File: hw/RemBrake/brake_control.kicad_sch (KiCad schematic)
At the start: 33 parts, among them J7 Conn_01x07, J8 Conn_01x07, J9 Conn_01x03, Q6 BC337, Q7 BC847, U5 LM555xN

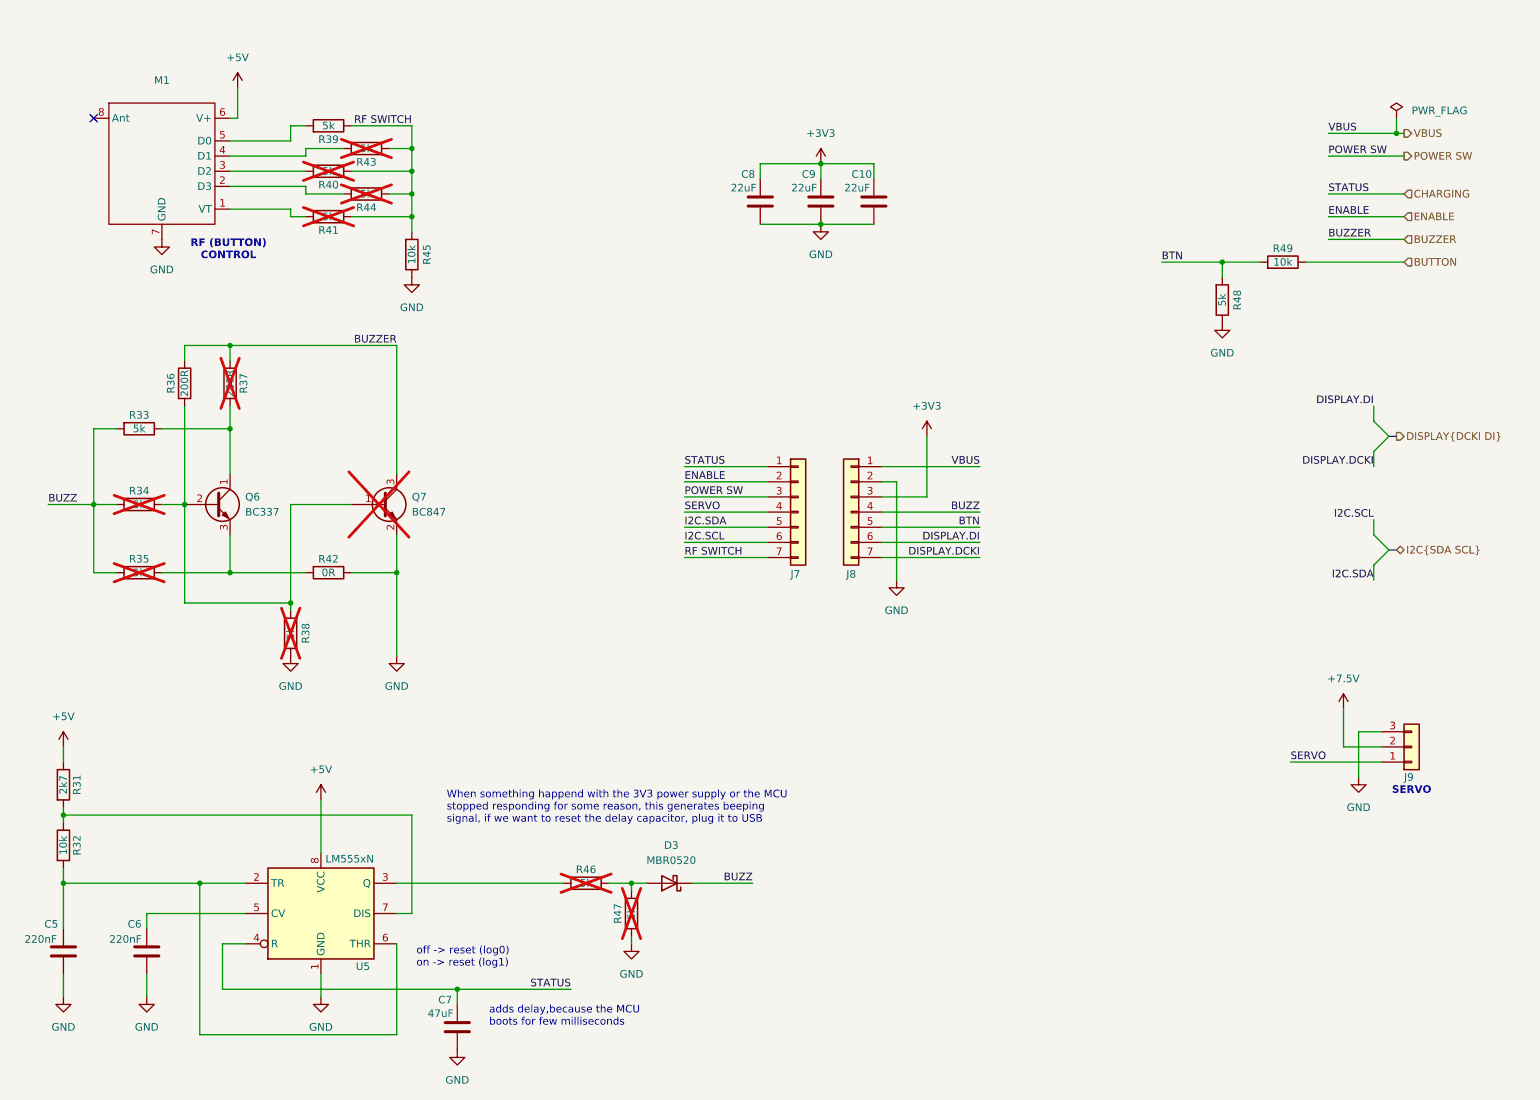
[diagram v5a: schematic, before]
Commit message: fixed bugs with LED reverse current leakage and beeper deterministic startup delay
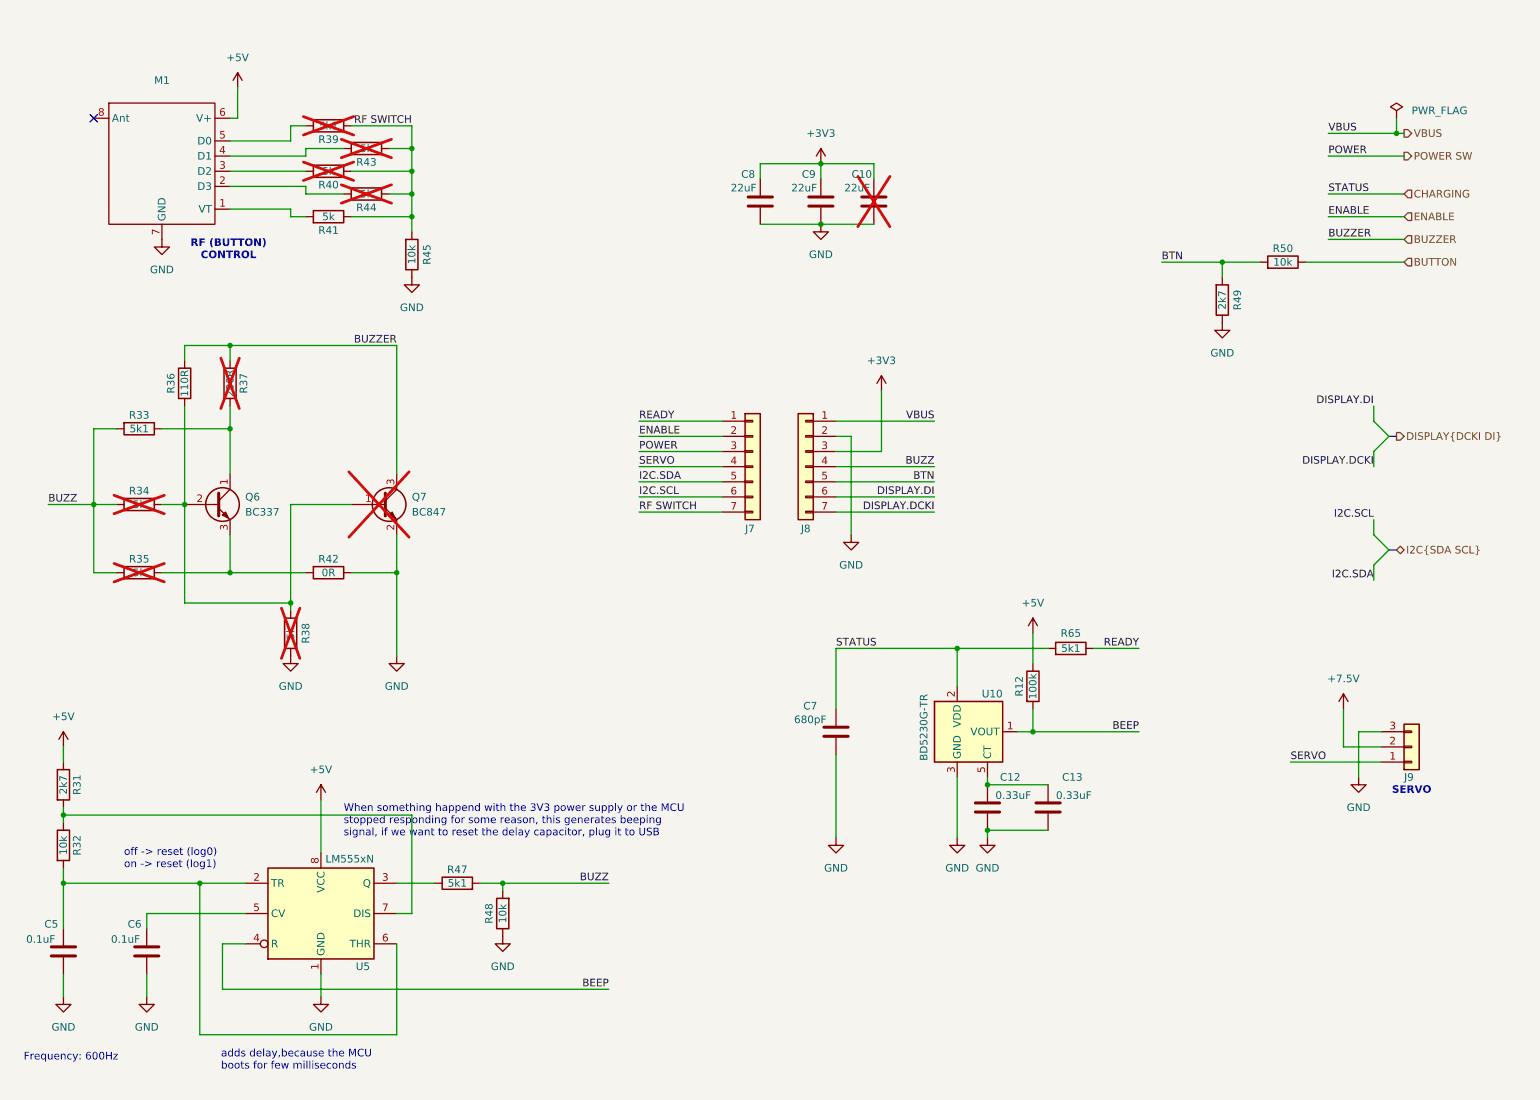
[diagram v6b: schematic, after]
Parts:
- removed D3: MBR0520, Diode_SMD:D_SOD-123, symbol Diode:MBR0520
- added C12, C13: 0.33uF, Capacitor_SMD:C_0805_2012Metric_Pad1.18x1.45mm_HandSolder, symbol Device:C
- added R12: 100k, Resistor_SMD:R_0805_2012Metric_Pad1.20x1.40mm_HandSolder, symbol Device:R
- added R65: 5k1, Resistor_SMD:R_0805_2012Metric_Pad1.20x1.40mm_HandSolder, symbol Device:R
- added U10: BD5230G-TR, Package_TO_SOT_SMD:SOT-23-6_Handsoldering, symbol dodo-power:BD5230G-TR
- C10: now not fitted
- C5, C6: value 220nF -> 0.1uF
- C7: value 47uF -> 680pF
- R33: value 5k -> 5k1
- R36: value 200R -> 110R
- R39: value 5k -> 5k1; now not fitted
- R41: now fitted
- R47: renamed from R46; value 5k -> 5k1; now fitted
- R48: renamed from R47; value 5k -> 10k; now fitted
- R49: renamed from R48; value 5k -> 2k7
- renumbered R49 to R50
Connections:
- net +5V: now also R12.1
- net BUZZ: now also R47.2, R48.2
- net CHARGING: now also R65.2, U10.2 (VDD); no longer J7.1 (Pin_1), U5.4 (R)
- net GND: now also C12.2, C13.2, U10.3 (GND)
- new net: C12.1, C13.1, U10.5 (CT)
- new net BEEP: R12.2, U10.1 (VOUT), U5.4 (R)
- new net READY: J7.1 (Pin_1), R65.1
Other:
- note added: "Frequency: 600Hz"
- moved on the sheet: J7, J8

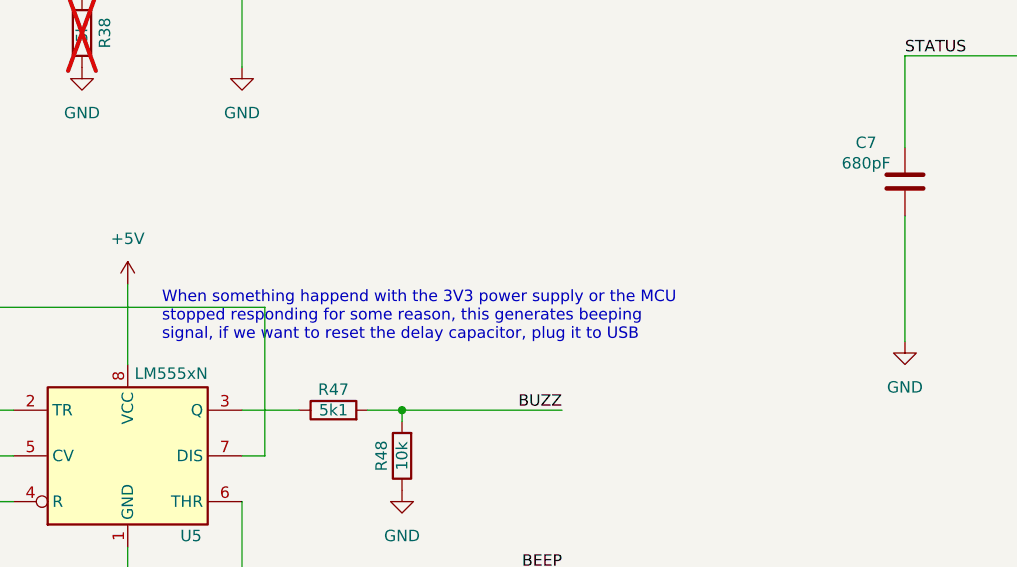
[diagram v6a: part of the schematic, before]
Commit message: updated pcb and added todo in the schematic
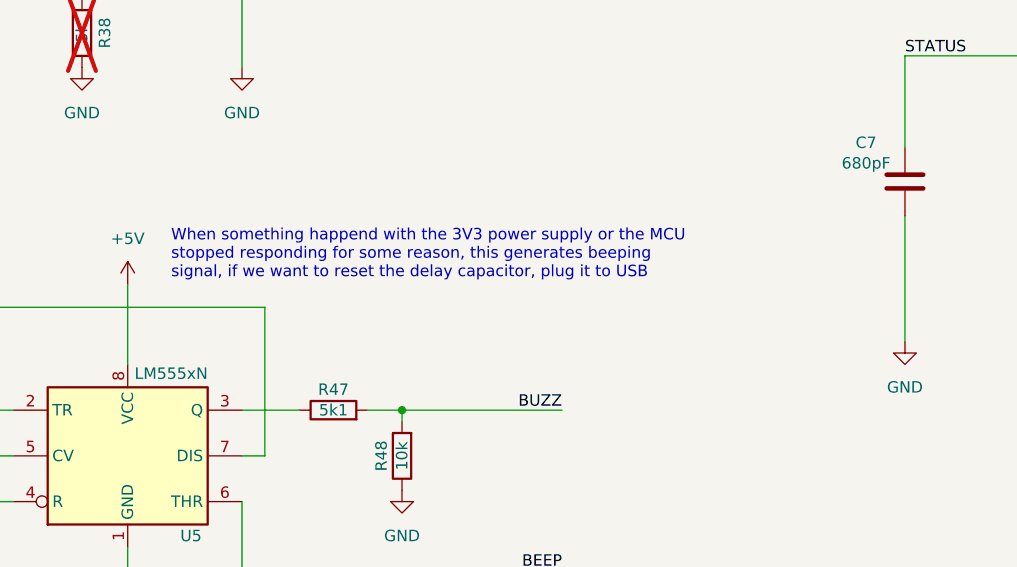
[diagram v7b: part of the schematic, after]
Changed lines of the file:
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@@
 	(text "When something happend with the 3V3 power supply or the MCU \nstopped responding for some reason, this generates beeping \nsignal, if we want to reset the delay capacitor, plug it to USB"
 		(exclude_from_sim no)
-		(at 74.93 152.146 0)
+		(at 75.946 145.288 0)
 		(effects
 			(font

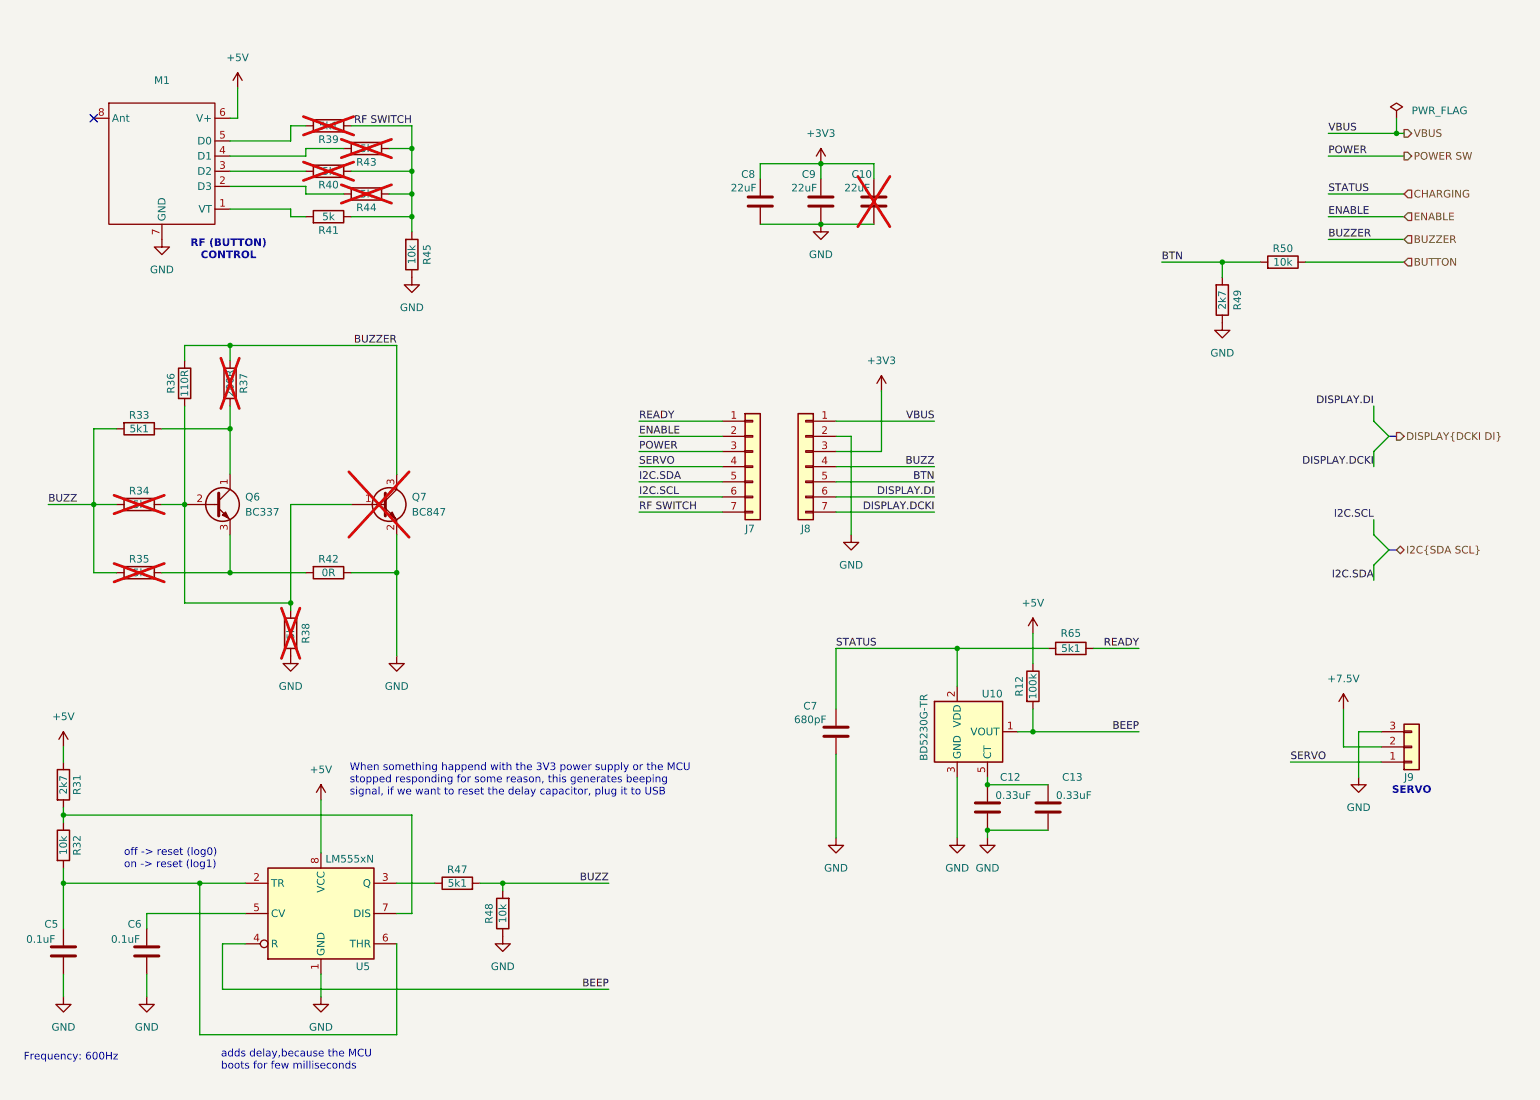
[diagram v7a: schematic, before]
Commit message: replaced optocoupler with transistor and loaded components in the pcb sheet
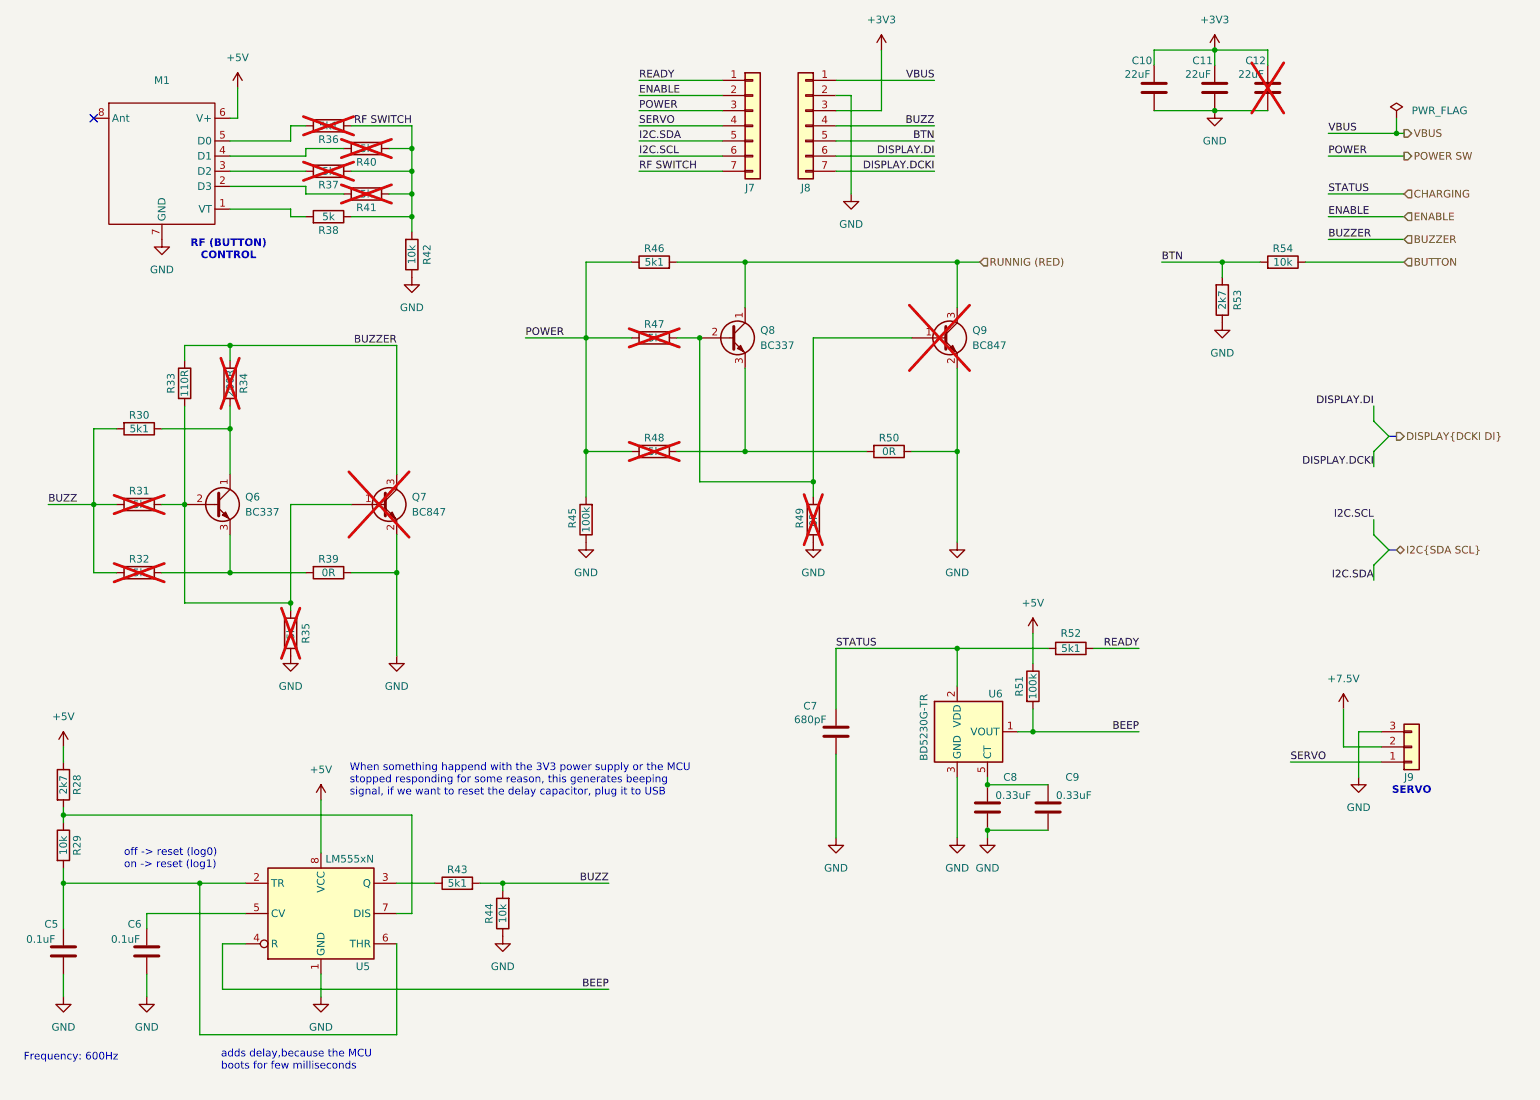
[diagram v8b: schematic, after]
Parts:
- added Q8: BC337, Package_TO_SOT_THT:TO-92_Inline, symbol Transistor_BJT:BC337
- added Q9: BC847, Package_TO_SOT_SMD:SOT-23, symbol Transistor_BJT:BC847
- added R45: 100k, Resistor_SMD:R_0805_2012Metric_Pad1.20x1.40mm_HandSolder, symbol Device:R
- added R46: 5k1, Resistor_SMD:R_0805_2012Metric_Pad1.20x1.40mm_HandSolder, symbol Device:R
- added R47, R48: 5k, Resistor_SMD:R_0805_2012Metric_Pad1.20x1.40mm_HandSolder, symbol Device:R
- added R49, R50: 0R, Resistor_SMD:R_0805_2012Metric_Pad1.20x1.40mm_HandSolder, symbol Device:R
- renumbered C8 to C10, C9 to C11, C10 to C12, C12 to C8, C13 to C9, R31 to R28, R32 to R29, R33 to R30, R34 to R31, R35 to R32, R36 to R33, R37 to R34, R38 to R35, R39 to R36, R40 to R37, R41 to R38, R42 to R39, R43 to R40, R44 to R41, R45 to R42, R47 to R43, R48 to R44, R12 to R51, R65 to R52, R49 to R53, R50 to R54, U10 to U6
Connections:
- net GND: now also Q9.2 (E), R45.1, R49.1, R50.1
- net POWER SW: now also R45.2, R46.1, R47.1, R48.1
- new net: Q8.2 (B), Q9.1 (B), R47.2, R49.2
- new net: Q8.3 (E), R48.2, R50.2
- new net RUNNIG (RED): Q8.1 (C), Q9.3 (C), R46.2
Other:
- moved on the sheet: C10, C11, C12, J7, J8
